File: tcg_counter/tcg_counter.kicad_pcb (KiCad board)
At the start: 2 copper layers, 0 parts

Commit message: Mess around with qr code on silkscreen
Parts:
- added QR*****: qrcode, Library:qrcode, F.Cu at (171.0, 55.0)
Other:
- board outline added: 63 x 88 mm
- board text added: "63x88mm Magic The Gathering Card dimensions 2mm corner fillet"

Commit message: Added contacts for display
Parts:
- added REF**: D0430G02V01, Library:D0430G02V01, F.Cu at (133.0, 100.0)
- moved QR***** 3.16 mm to (172.0, 52.0)
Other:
- board text added: "groundst8"
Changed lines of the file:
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@@
 	)
 	(net 0 "")
+	(footprint "Library:D0430G02V01"
+		(layer "F.Cu")
+		(at 133 100)
+		(property "Reference" "REF**"
+			(at 17.5 -0.5 0)
+			(unlocked yes)
+			(layer "F.SilkS")
+			(effects
+				(font
+					(size 1 1)
+					(thickness 0.1)
+				)
+			)
+		)
+		(property "Value" "D0430G02V01"
+			(at 17.5 1 0)
+			(unlocked yes)
+			(layer "F.Fab")
+			(effects
+				(font
+					(size 1 1)
+					(thickness 0.15)
+				)
+			)
+		)
+		(property "Footprint" "Library:D0430G02V01"
+			(at 17.5 0 0)
+			(unlocked yes)
+			(layer "F.Fab")
+			(hide yes)
+			(effects
+				(font
+					(size 1 1)
+					(thickness 0.15)
+				)
+			)
+		)
+		(property "Datasheet" ""
+			(at 17.5 0 0)
+			(unlocked yes)
+			(layer "F.Fab")
+			(hide yes)
+			(effects
+				(font
+					(size 1 1)
+					(thickness 0.15)
+				)
+			)
+		)
+		(property "Description" ""
+			(at 17.5 0 0)
+			(unlocked yes)
+			(layer "F.Fab")
+			(hide yes)
+			(effects
+				(font
+					(size 1 1)
+					(thickness 0.15)
+				)
+			)
+		)
+		(attr smd)
+		(fp_line
+			(start -5.3 -5.05)
+			(end -5.3 -28.95)
+			(stroke
+				(width 0.1)
+				(type default)
+			)
+			(layer "F.SilkS")
+		)
+		(fp_line
+			(start -0.3 -33.95)
+			(end 35.3 -33.95)
+			(stroke
+				(width 0.1)
+				(type default)
+			)
+			(layer "F.SilkS")
+		)
+		(fp_line
+			(start 35.3 -0.05)
+			(end -0.3 -0.05)
+			(stroke
+				(width 0.1)
+				(type default)
+			)
+			(layer "F.SilkS")
+		)
+		(fp_line
+			(start 40.3 -28.95)
+			(end 40.3 -5.05)
+			(stroke
+				(width 0.1)
+				(type default)
+			)
+			(layer "F.SilkS")
+		)
+		(fp_rect
+			(start 9 0)
+			(end 26 12.2)
+			(stroke
+				(width 0.1)
+				(type default)
+			)
+			(fill none)
+			(layer "F.SilkS")
+		)
+		(fp_arc
+			(start -5.3 -28.95)
+			(mid -3.835534 -32.485534)
+			(end -0.3 -33.95)
+			(stroke
+				(width 0.1)
+				(type default)
+			)
+			(layer "F.SilkS")
+		)
+		(fp_arc
+			(start -0.3 -0.05)
+			(mid -3.835534 -1.514466)
+			(end -5.3 -5.05)
+			(stroke
+				(width 0.1)
+				(type default)
+			)
+			(layer "F.SilkS")
+		)
+		(fp_arc
+			(start 35.3 -33.95)
+			(mid 38.835534 -32.485534)
+			(end 40.3 -28.95)
+			(stroke
+				(width 0.1)
+				(type default)
+			)
+			(layer "F.SilkS")
+		)
+		(fp_arc
+			(start 40.3 -5.05)
+			(mid 38.835534 -1.514466)
+			(end 35.3 -0.05)
+			(stroke
+				(width 0.1)
+				(type default)
+			)
+			(layer "F.SilkS")
+		)
+		(fp_text user "${REFERENCE}"
+			(at 17.5 2.5 0)
+			(unlocked yes)
+			(layer "F.Fab")
+			(effects
+				(font
+					(size 1 1)
+					(thickness 0.15)
+				)
+			)
+		)
+		(group ""
+			(members "1877cc40-3a08-4af4-9a8c-e5f6e10205c6" "2965150a-dffd-4d5a-b026-78367372da49"
+				"2d1dd96f-1437-487e-979a-3712ffb07f32" "499c2ffa-4a00-46bf-af79-cfc733f626d7"
+				"7a005273-b8f0-4762-9940-fb704984a0e7" "b155dca7-d10d-4cfd-8d2a-33f6957ffbaf"
+				"c10cf675-66a3-4e8d-9314-a9d3754c2392" "fb935753-c1e5-47dc-bc01-6c810b15662e"
+			)
+		)
+	)
 	(footprint "Library:qrcode"
 		(layer "F.Cu")
-		(at 171 55)
+		(at 172 52)
 		(property "Reference" "QR*****"
 			(at 0 9.75 0)
 			(layer "F.SilkS")
+			(hide yes)
 			(effects
 				(font
@@
 			(at 0 -9.75 0)
 			(layer "F.SilkS")
+			(hide yes)
 			(effects
 				(font
@@
 		(layer "Edge.Cuts")
 	)
+	(gr_text "groundst8"
+		(at 125 47 0)
+		(layer "F.SilkS")
+		(effects
+			(font
+				(size 2 2)
+				(thickness 0.3)
+			)
+			(justify left bottom)
+		)
+	)
 	(gr_text "63x88mm Magic The Gathering Card dimensions\n2mm corner fillet"

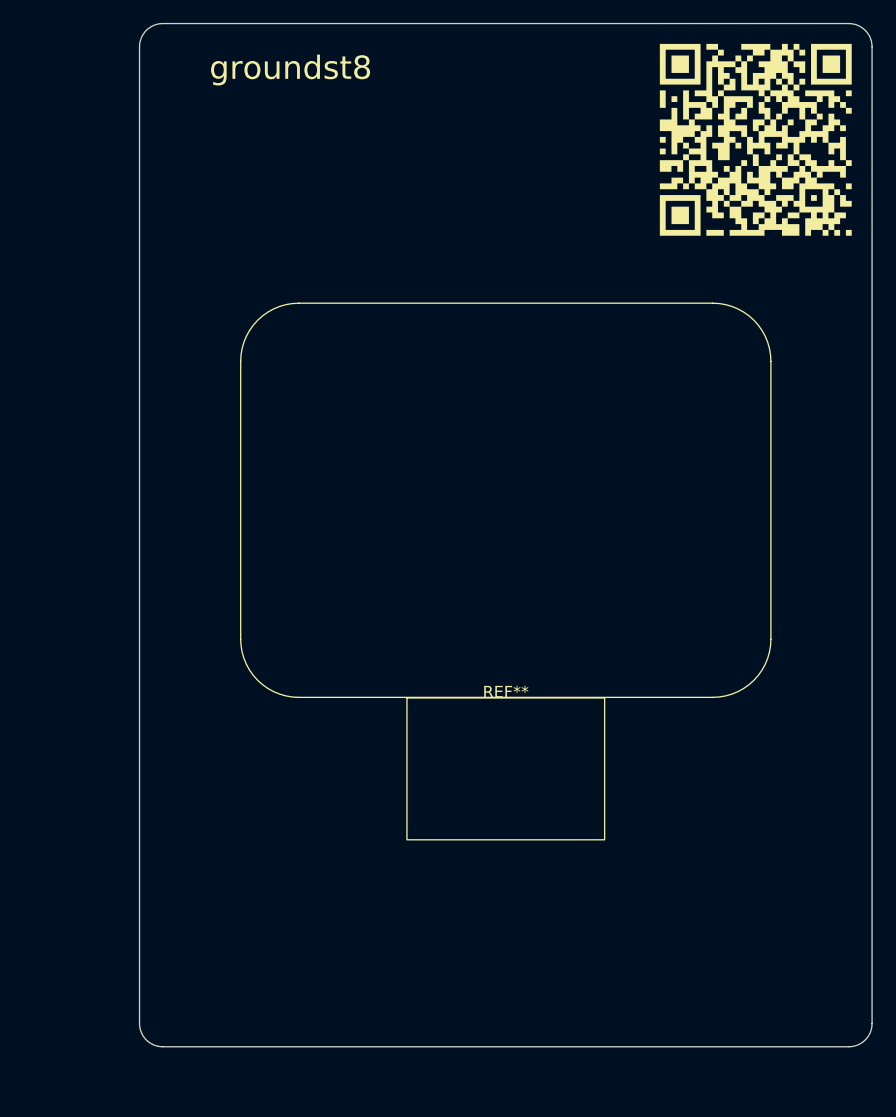
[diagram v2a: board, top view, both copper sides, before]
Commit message: Added dispay symbol to schematic and update TCAL9539
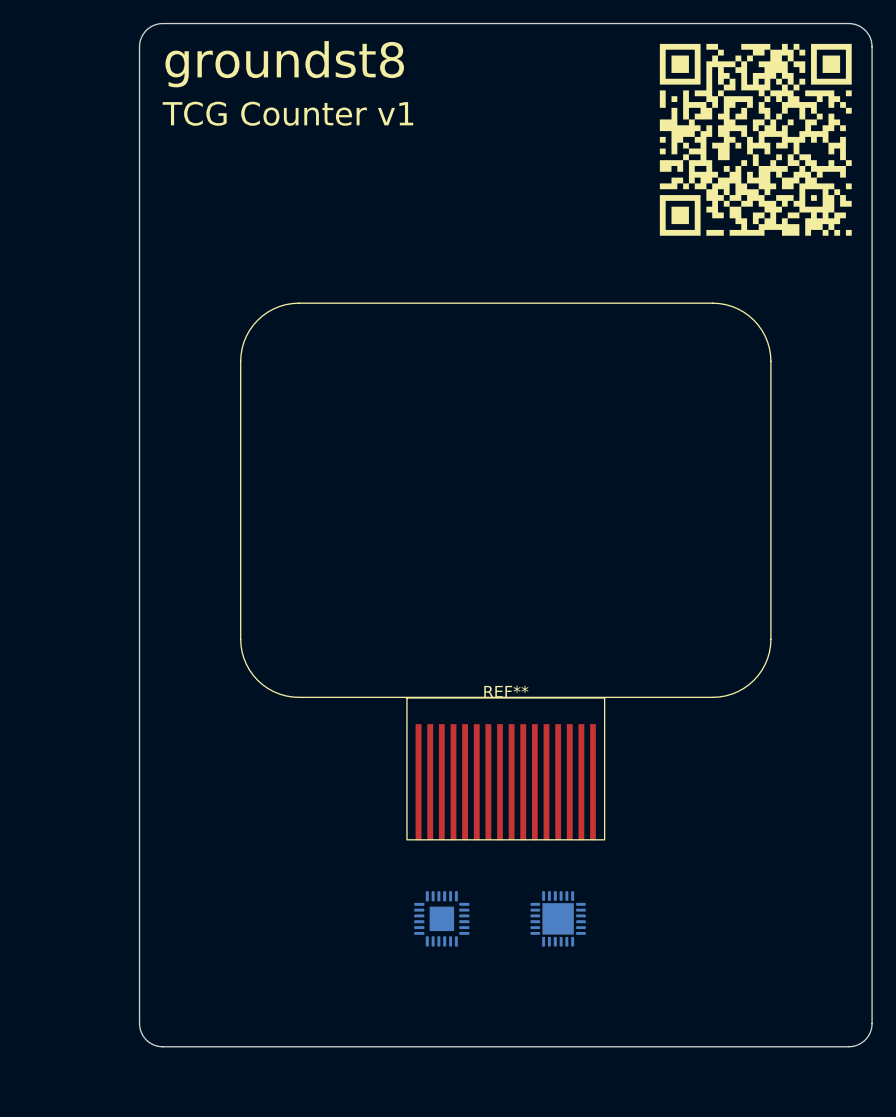
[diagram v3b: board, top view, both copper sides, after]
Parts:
- added REF**: Texas_RTW_WQFN-24-1EP_4x4mm_P0.5mm_EP2.7x2.7mm, Package_DFN_QFN:Texas_RTW_WQFN-24-1EP_4x4mm_P0.5mm_EP2.7x2.7mm, B.Cu at (155.0, 119.0)
- added REF**: Texas_RGE0024C_VQFN-24-1EP_4x4mm_P0.5mm_EP2.1x2.1mm, Package_DFN_QFN:Texas_RGE0024C_VQFN-24-1EP_4x4mm_P0.5mm_EP2.1x2.1mm, B.Cu at (145.0, 119.0)
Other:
- board text added: "TCG Counter v1"

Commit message: Added antenna trace from goodtag
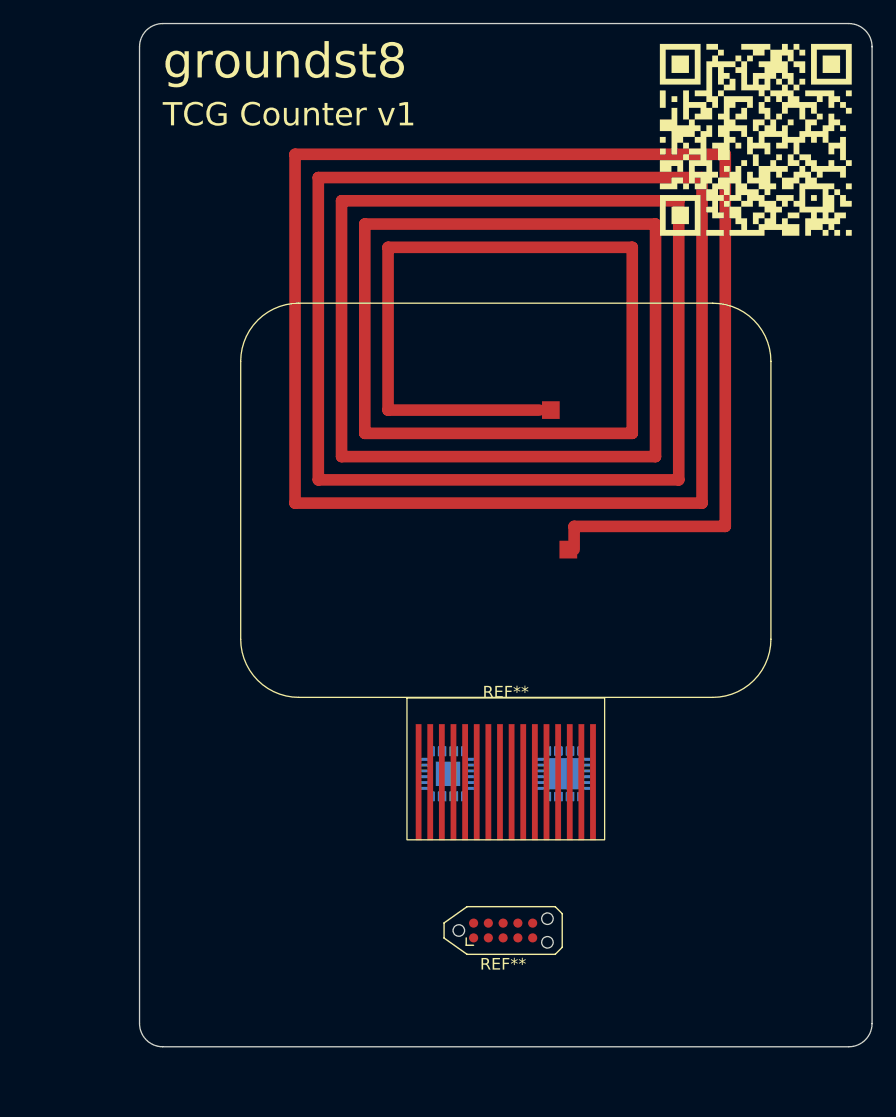
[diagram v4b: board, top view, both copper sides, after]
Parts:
- added L1: Antenna, footprints:GW10ANT, F.Cu at (130.4, 52.2)
- added REF**: Tag-Connect_TC2050-IDC-NL_2x05_P1.27mm_Vertical_with_bottom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, Connector:Tag-Connect_TC2050-IDC-NL_2x05_P1.27mm_Vertical_with_bottom_clip, F.Cu at (150.3, 120.0)
- moved REF** 12.5 mm to (155.5, 106.5)
- moved REF** 12.5 mm to (145.5, 106.5)

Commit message: Removed QR code
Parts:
- removed QR*****: qrcode, Library:qrcode

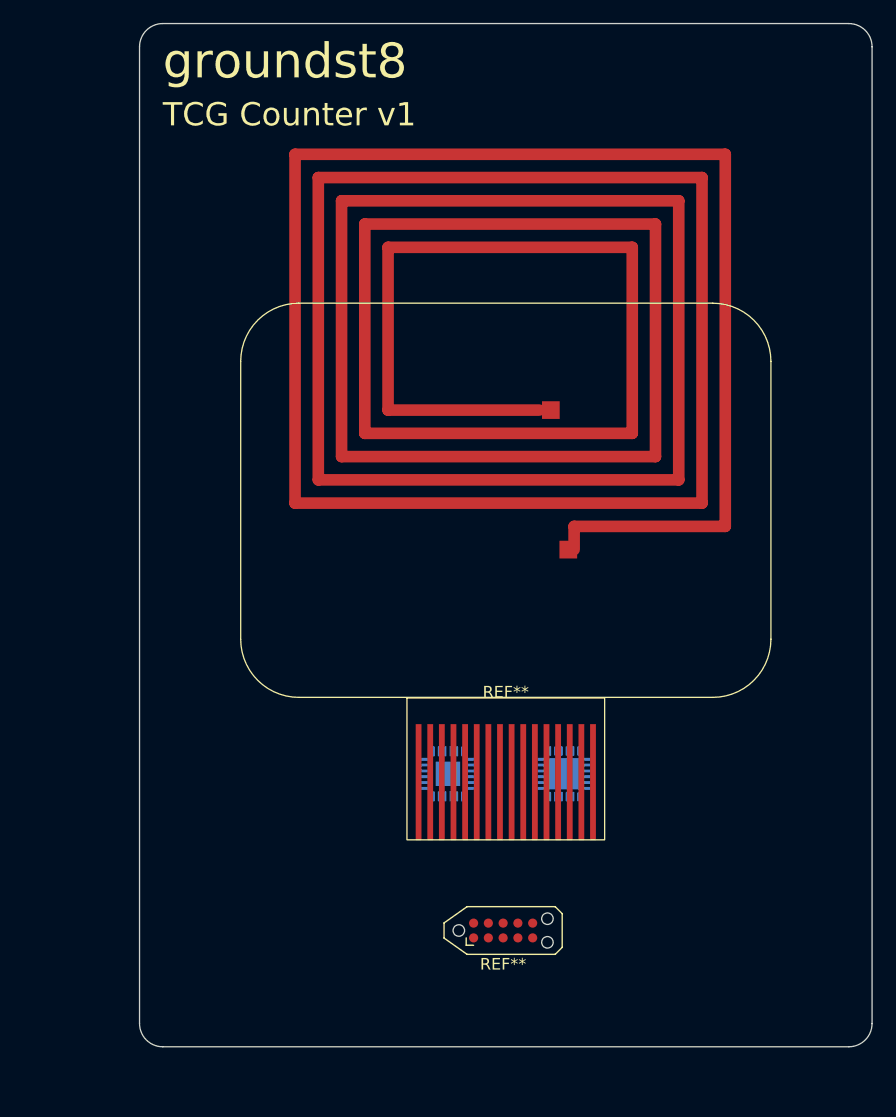
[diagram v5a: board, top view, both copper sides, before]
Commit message: Added current limiting resistor
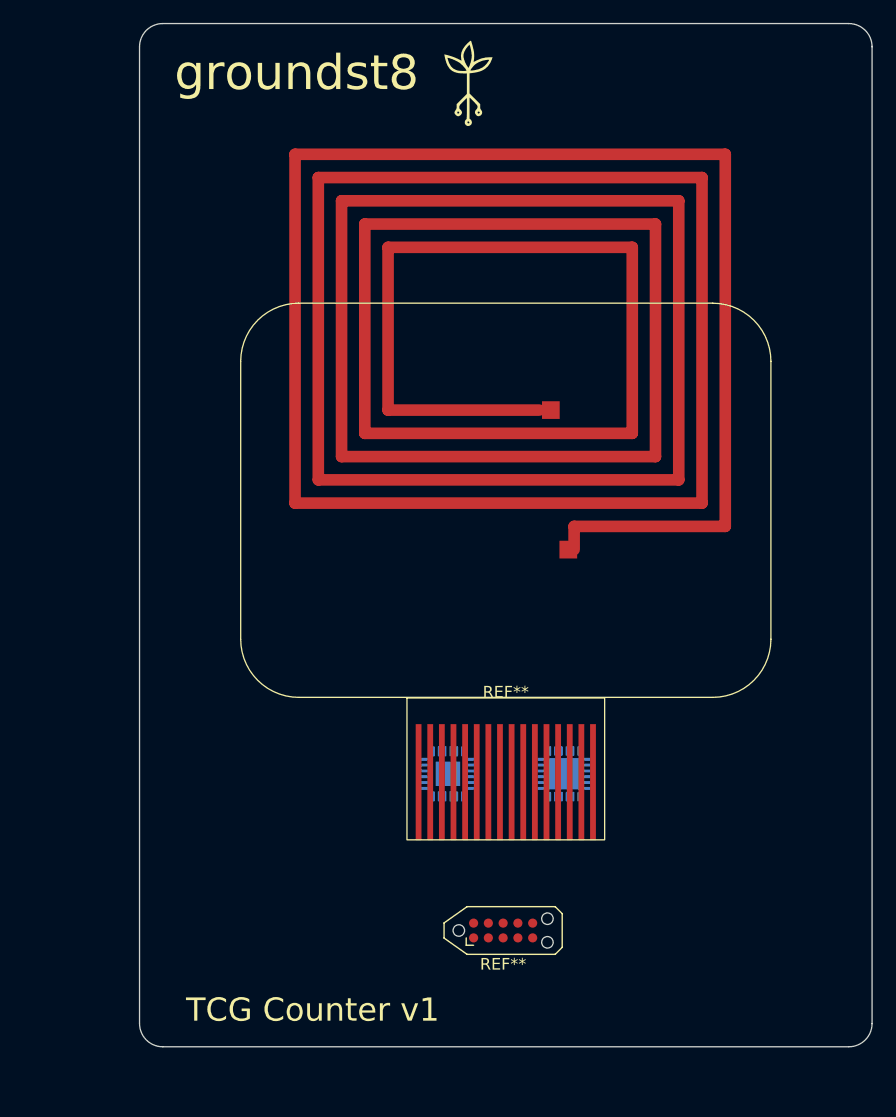
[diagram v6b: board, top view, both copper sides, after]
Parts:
- added G***: LOGO, LOGO, F.Cu at (147.0, 47.0)
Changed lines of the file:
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@@
+		)
+	)
+	(footprint "LOGO"
+		(layer "F.Cu")
+		(at 147 47)
+		(property "Reference" "G***"
+			(at 0 0 0)
+			(layer "F.SilkS")
+			(hide yes)
+			(effects
+				(font
+					(size 1.5 1.5)
+					(thickness 0.3)
+				)
+			)
+		)
+		(property "Value" "LOGO"
+			(at 0.75 0 0)
+			(layer "F.SilkS")
+			(hide yes)
+			(effects
+				(font
+					(size 1.5 1.5)
+					(thickness 0.3)
+				)
+			)
+		)
+		(property "Footprint" ""
+			(at 0 0 0)
+			(layer "F.Fab")
+			(hide yes)
+			(effects
+				(font
+					(size 1.27 1.27)
+					(thickness 0.15)
+				)
+			)
+		)
+		(property "Datasheet" ""
+			(at 0 0 0)
+			(layer "F.Fab")
+			(hide yes)
+			(effects
+				(font
+					(size 1.27 1.27)
+					(thickness 0.15)
+				)
+			)
+		)
+		(property "Description" ""
+			(at 0 0 0)
+			(layer "F.Fab")
+			(hide yes)
+			(effects
+				(font
+					(size 1.27 1.27)
+					(thickness 0.15)
+				)
+			)
+		)
+		(attr board_only exclude_from_pos_files exclude_from_bom)
+		(fp_poly
+			(pts
+				(xy 0.525925 -3.470921) (xy 0.56503 -3.357513) (xy 0.610798 -3.203575) (xy 0.658597 -3.0262) (xy 0.703796 -2.842478)
+				(xy 0.741764 -2.669502) (xy 0.765476 -2.54) (xy 0.788018 -2.233254) (xy 0.766323 -1.918762) (xy 0.737651 -1.765788)
+				(xy 0.732109 -1.726345) (xy 0.747834 -1.71246) (xy 0.796856 -1.727207) (xy 0.89121 -1.773659) (xy 1.003843 -1.833787)
+				(xy 1.378204 -1.992812) (xy 1.780046 -2.080727) (xy 2.088698 -2.100089) (xy 2.363111 -2.100752)
+				(xy 2.285208 -1.870069) (xy 2.145926 -1.572747) (xy 1.94463 -1.306982) (xy 1.693619 -1.086644) (xy 1.476033 -0.957554)
+				(xy 1.296124 -0.887732) (xy 1.06552 -0.823813) (xy 0.809915 -0.77209) (xy 0.601578 -0.74339) (xy 0.381954 -0.720218)
+				(xy 0.381954 0.146578) (xy 0.381954 1.013374) (xy 0.8403 1.470526) (xy 1.298646 1.927678) (xy 1.298646 2.135888)
+				(xy 1.307271 2.278533) (xy 1.338423 2.374248) (xy 1.382676 2.433545) (xy 1.457851 2.560624) (xy 1.467485 2.695586)
+				(xy 1.417929 2.820489) (xy 1.315536 2.91739) (xy 1.195006 2.96369) (xy 1.104775 2.970236) (xy 1.030224 2.937851)
+				(xy 0.956417 2.872068) (xy 0.860637 2.737224) (xy 0.848421 2.654662) (xy 1.075518 2.654662) (xy 1.101335 2.71734)
+				(xy 1.161377 2.744304) (xy 1.173957 2.74291) (xy 1.237702 2.698865) (xy 1.253286 2.663581) (xy 1.235813 2.599282)
+				(xy 1.176893 2.566443) (xy 1.109911 2.581168) (xy 1.10003 2.589654) (xy 1.075518 2.654662) (xy 0.848421 2.654662)
+				(xy 0.840694 2.602436) (xy 0.8966 2.471237) (xy 0.954887 2.406315) (xy 1.041785 2.297786) (xy 1.069386 2.17907)
+				(xy 1.069473 2.17057) (xy 1.062794 2.109415) (xy 1.036882 2.046805) (xy 0.982926 1.97067) (xy 0.892113 1.868939)
+				(xy 0.755631 1.729543) (xy 0.725714 1.699699) (xy 0.381954 1.357532) (xy 0.381954 2.265711) (xy 0.381954 3.173889)
+				(xy 0.480983 3.25907) (xy 0.56624 3.376937) (xy 0.589051 3.514613) (xy 0.549317 3.648703) (xy 0.483022 3.72895)
+				(xy 0.346067 3.805478) (xy 0.205688 3.810828) (xy 0.076453 3.745107) (xy 0.055557 3.725796) (xy -0.014996 3.609027)
+				(xy -0.028603 3.496761) (xy 0.198153 3.496761) (xy 0.203804 3.530515) (xy 0.255414 3.58236) (xy 0.325598 3.58225)
+				(xy 0.365122 3.548515) (xy 0.366235 3.490771) (xy 0.323304 3.437674) (xy 0.263704 3.412835) (xy 0.224374 3.427114)
+				(xy 0.198153 3.496761) (xy -0.028603 3.496761) (xy -0.031533 3.472582) (xy 0.003559 3.342185) (xy 0.087896 3.24356)
+				(xy 0.101064 3.235169) (xy 0.118083 3.210515) (xy 0.131131 3.153759) (xy 0.14066 3.056777) (xy 0.147119 2.911446)
+				(xy 0.150956 2.709641) (xy 0.152621 2.443237) (xy 0.152781 2.300223) (xy 0.152781 1.395821) (xy -0.17188 1.718797)
+				(xy -0.310026 1.857937) (xy -0.402272 1.957876) (xy -0.457821 2.032319) (xy -0.485875 2.094974)
+				(xy -0.495636 2.159546) (xy -0.496542 2.202372) (xy -0.487415 2.314052) (xy -0.454924 2.370844)
+				(xy -0.425947 2.385378) (xy -0.352712 2.442435) (xy -0.294516 2.545668) (xy -0.267702 2.664872)
+				(xy -0.267369 2.678419) (xy -0.299096 2.769731) (xy -0.378065 2.865239) (xy -0.479956 2.942409)
+				(xy -0.580449 2.978706) (xy -0.592031 2.979248) (xy -0.697681 2.947502) (xy -0.80309 2.868055) (xy -0.884135 2.764596)
+				(xy -0.916692 2.660813) (xy -0.916692 2.660455) (xy -0.915171 2.654662) (xy -0.681475 2.654662)
+				(xy -0.655658 2.71734) (xy -0.595615 2.744304) (xy -0.583036 2.74291) (xy -0.51929 2.698865) (xy -0.503706 2.663581)
+				(xy -0.52118 2.599282) (xy -0.5801 2.566443) (xy -0.647082 2.581168) (xy -0.656963 2.589654) (xy -0.681475 2.654662)
+				(xy -0.915171 2.654662) (xy -0.892511 2.568374) (xy -0.833117 2.466379) (xy -0.821203 2.451476)
+				(xy -0.759738 2.35873) (xy -0.731358 2.251491) (xy -0.725715 2.13281) (xy -0.725715 1.927626) (xy -0.286467 1.489624)
+				(xy 0.152781 1.051622) (xy 0.152754 0.172502) (xy 0.152727 -0.706617) (xy -0.238749 -0.710858) (xy -0.578256 -0.736139)
+				(xy -0.868069 -0.80686) (xy -1.112407 -0.92723) (xy -1.315489 -1.101455) (xy -1.481532 -1.333744)
+				(xy -1.614756 -1.628303) (xy -1.719378 -1.989339) (xy -1.73419 -2.062257) (xy -1.520827 -2.062257)
+				(xy -1.472304 -1.880978) (xy -1.363443 -1.571465) (xy -1.218026 -1.326746) (xy -1.032094 -1.142528)
+				(xy -0.801687 -1.014518) (xy -0.62127 -0.958251) (xy -0.512289 -0.940428) (xy -0.373058 -0.928309)
+				(xy -0.222723 -0.922089) (xy -0.08043 -0.921967) (xy 0.034675 -0.928139) (xy 0.103447 -0.940802)
+				(xy 0.114586 -0.950686) (xy 0.104565 -0.976652) (xy 0.458345 -0.976652) (xy 0.481461 -0.959301)
+				(xy 0.556352 -0.957939) (xy 0.691334 -0.972962) (xy 0.83215 -0.994431) (xy 1.177586 -1.077044) (xy 1.464429 -1.204128)
+				(xy 1.664137 -1.34714) (xy 1.762497 -1.444366) (xy 1.865133 -1.562651) (xy 1.95833 -1.683925) (xy 2.028374 -1.79012)
+				(xy 2.061551 -1.863169) (xy 2.062556 -1.872047) (xy 2.028575 -1.882235) (xy 1.940208 -1.879304)
+				(xy 1.817816 -1.865893) (xy 1.681761 -1.844642) (xy 1.552403 -1.818191) (xy 1.466641 -1.794806)
+				(xy 1.227347 -1.699293) (xy 1.000519 -1.576472) (xy 0.820371 -1.445575) (xy 0.738565 -1.363908)
+				(xy 0.646934 -1.25801) (xy 0.560131 -1.146859) (xy 0.492806 -1.049432) (xy 0.459613 -0.984709) (xy 0.458345 -0.976652)
+				(xy 0.104565 -0.976652) (xy 0.088128 -1.019241) (xy 0.017362 -1.123663) (xy -0.084802 -1.249205)
+				(xy -0.205454 -1.381119) (xy -0.331685 -1.504661) (xy -0.450584 -1.605083) (xy -0.472321 -1.621076)
+				(xy -0.667416 -1.740447) (xy -0.907839 -1.857974) (xy -1.16339 -1.96036) (xy -1.403871 -2.034305)
+				(xy -1.419286 -2.038055) (xy -1.520827 -2.062257) (xy -1.73419 -2.062257) (xy -1.769891 -2.238011)
+				(xy -1.790889 -2.356171) (xy -1.382437 -2.247592) (xy -1.167321 -2.182261) (xy -0.934772 -2.09863)
+				(xy -0.722032 -2.010543) (xy -0.638814 -1.971205) (xy -0.303643 -1.803398) (xy -0.332105 -1.942526)
+				(xy -0.358783 -2.232312) (xy -0.346389 -2.313929) (xy -0.139182 -2.313929) (xy -0.136585 -2.132498)
+				(xy -0.090415 -1.91529) (xy -0.007369 -1.684046) (xy 0.105853 -1.460508) (xy 0.141385 -1.403282)
+				(xy 0.284394 -1.183256) (xy 0.354481 -1.31987) (xy 0.39884 -1.425439) (xy 0.449519 -1.574482) (xy 0.496023 -1.735958)
+				(xy 0.49875 -1.746532) (xy 0.535808 -1.916533) (xy 0.562403 -2.086424) (xy 0.572923 -2.220168) (xy 0.572932 -2.223059)
+				(xy 0.563031 -2.370258) (xy 0.536923 -2.559577) (xy 0.500001 -2.761573) (xy 0.457659 -2.9468) (xy 0.41529 -3.085815)
+				(xy 0.414549 -3.087742) (xy 0.375271 -3.189324) (xy 0.221669 -3.017444) (xy 0.05267 -2.79333) (xy -0.070614 -2.556587)
+				(xy -0.136935 -2.329139) (xy -0.139182 -2.313929) (xy -0.346389 -2.313929) (xy -0.316324 -2.511922)
+				(xy -0.202915 -2.786055) (xy -0.016743 -3.059405) (xy 0.183357 -3.278268) (xy 0.302914 -3.390738)
+				(xy 0.403825 -3.475353) (xy 0.473615 -3.522268) (xy 0.498113 -3.526707)
+			)
+			(stroke
+				(width 0)
+				(type solid)
+			)
+			(fill solid)
+			(layer "F.SilkS")
 		)
 	)
@@
 	)
 	(gr_text "groundst8"
-		(at 121 47 0)
+		(at 122 48 0)
 		(layer "F.SilkS")
 		(effects
@@
 	)
 	(gr_text "TCG Counter v1"
-		(at 121 51 0)
+		(at 123 128 0)
 		(layer "F.SilkS")
 		(effects
